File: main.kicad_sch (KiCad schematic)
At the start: 2 parts

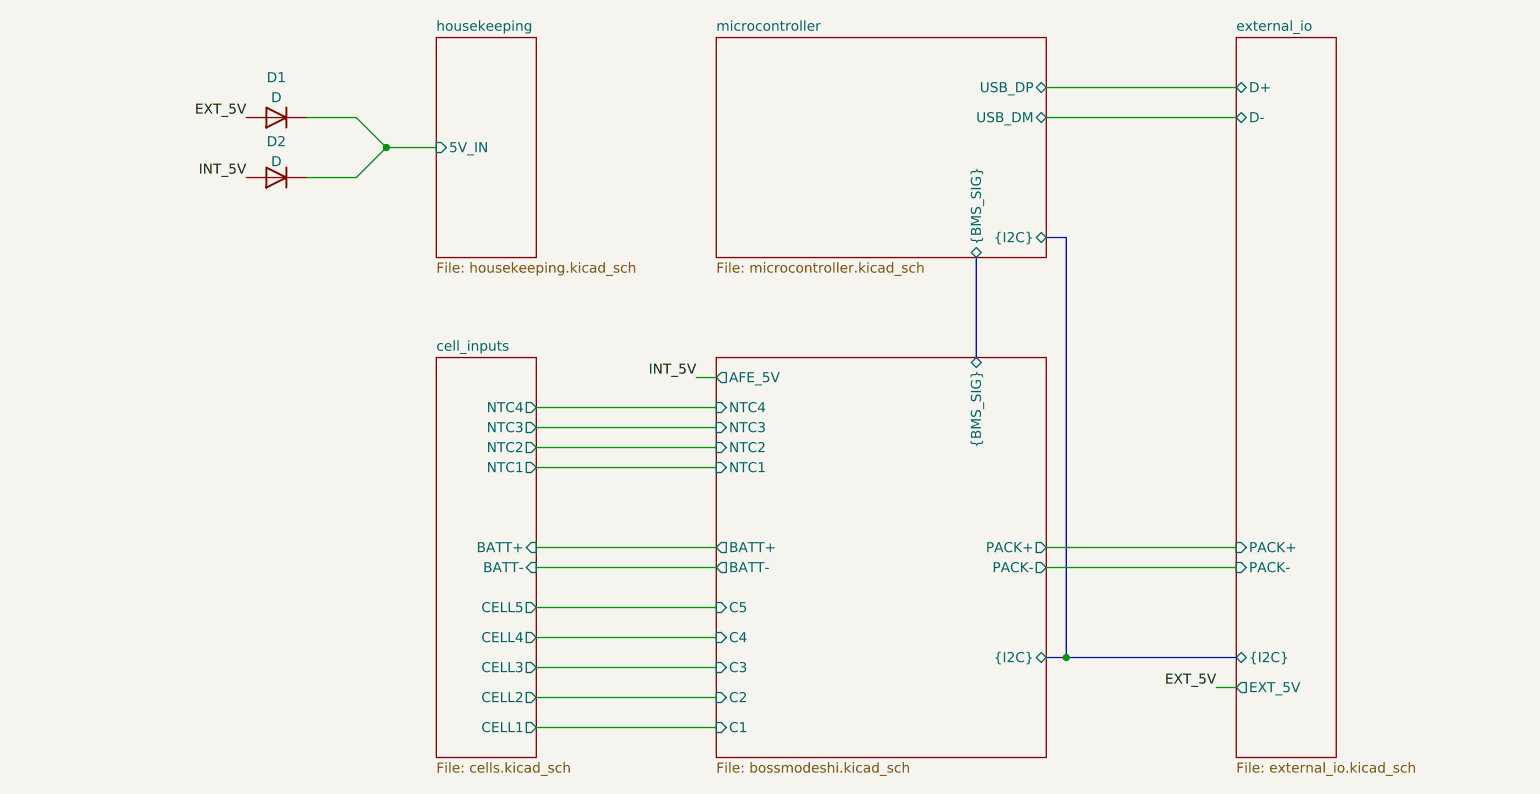
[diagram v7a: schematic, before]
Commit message: Adding proper grounding
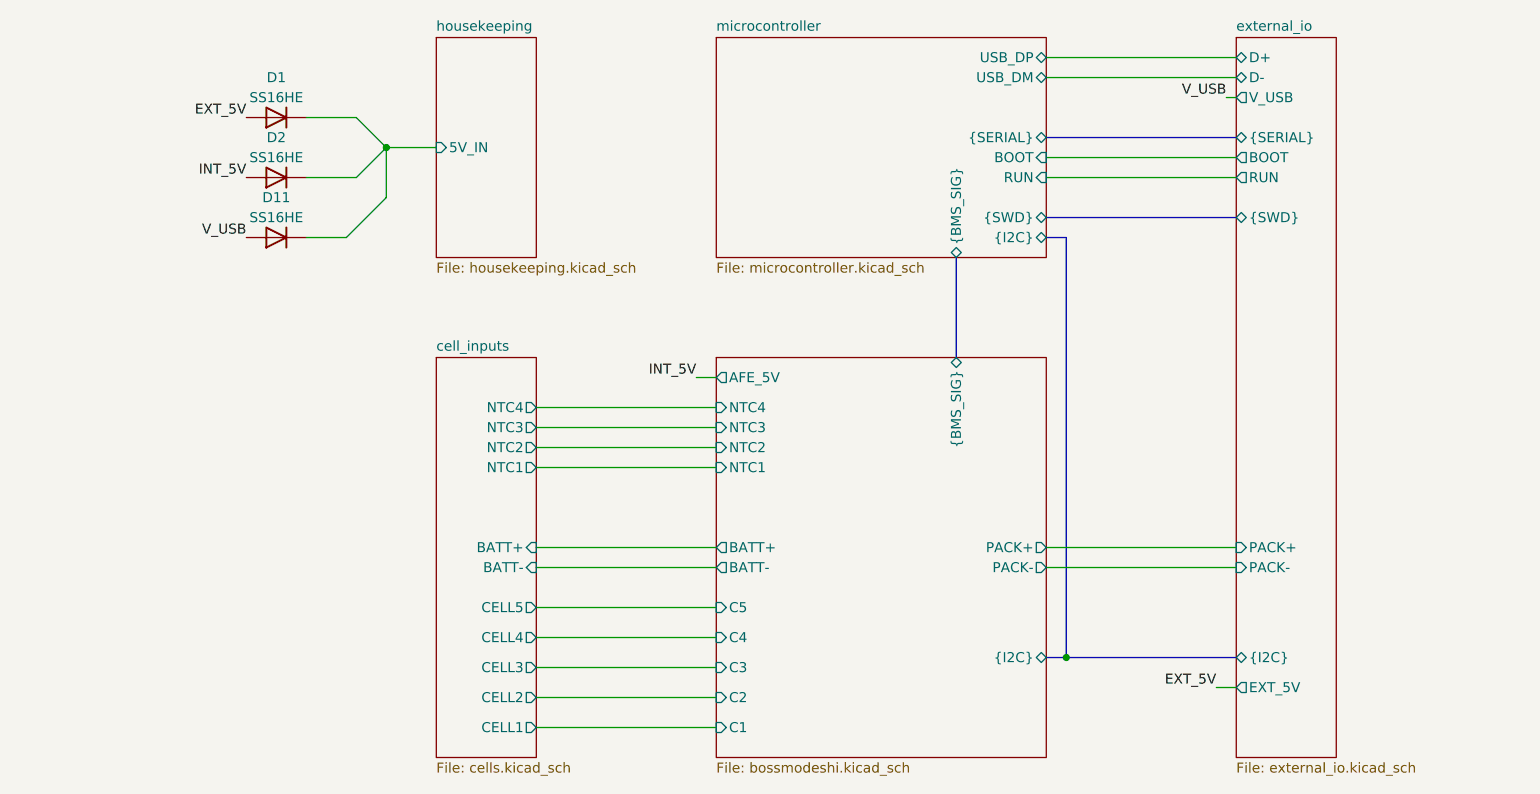
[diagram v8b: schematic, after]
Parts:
- added D11: SS16HE, Diode_SMD:D_SOD-323F, symbol Device:D
- D1, D2: value D -> SS16HE; footprint (none) -> Diode_SMD:D_SOD-323F; Mfr (none) -> onsemi; Mfr P/N (none) -> SS16HE; Supplier_1 (none) -> Digikey; Supplier_1 P/N (none) -> SS16HETR-ND; Supplier_1 Price @ Qty (none) -> 1; Supplier_1 Unit Price (none) -> 0.19000
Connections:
- net housekeeping/5V_IN: now also D11.1 (K)
- new net V_USB: D11.2 (A)
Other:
- sheet external_io ports: added BOOT, RUN, V_USB, {SERIAL}, {SWD}; removed none
- sheet microcontroller ports: added BOOT, RUN, {SERIAL}, {SWD}; removed none
